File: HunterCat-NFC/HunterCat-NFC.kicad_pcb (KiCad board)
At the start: 2 copper layers, 116.6 x 40.1 mm, 59 parts, among them U1 ATSAMD21E18A, U2 PN7150B0HN/C11004, U3 MCP73831-3-OT, U4 AP2112K-3.3, U5 W25Q32JVSS

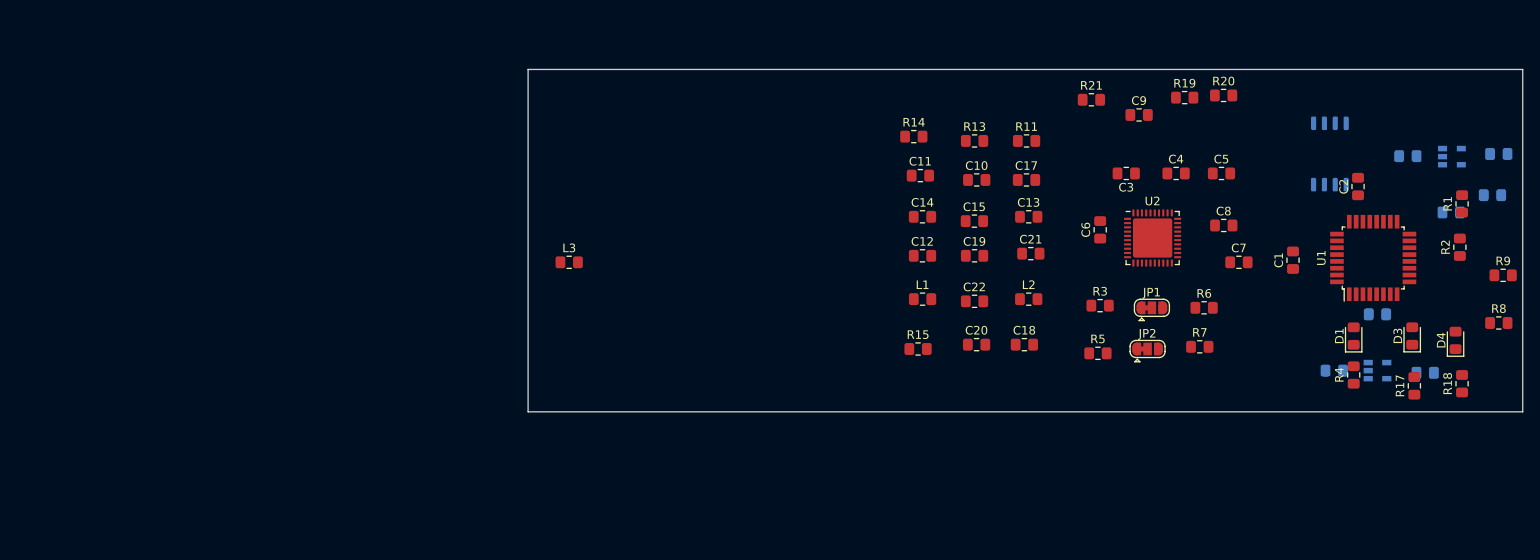
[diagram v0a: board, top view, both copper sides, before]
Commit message: Update libraries, add antenna 30x30mm
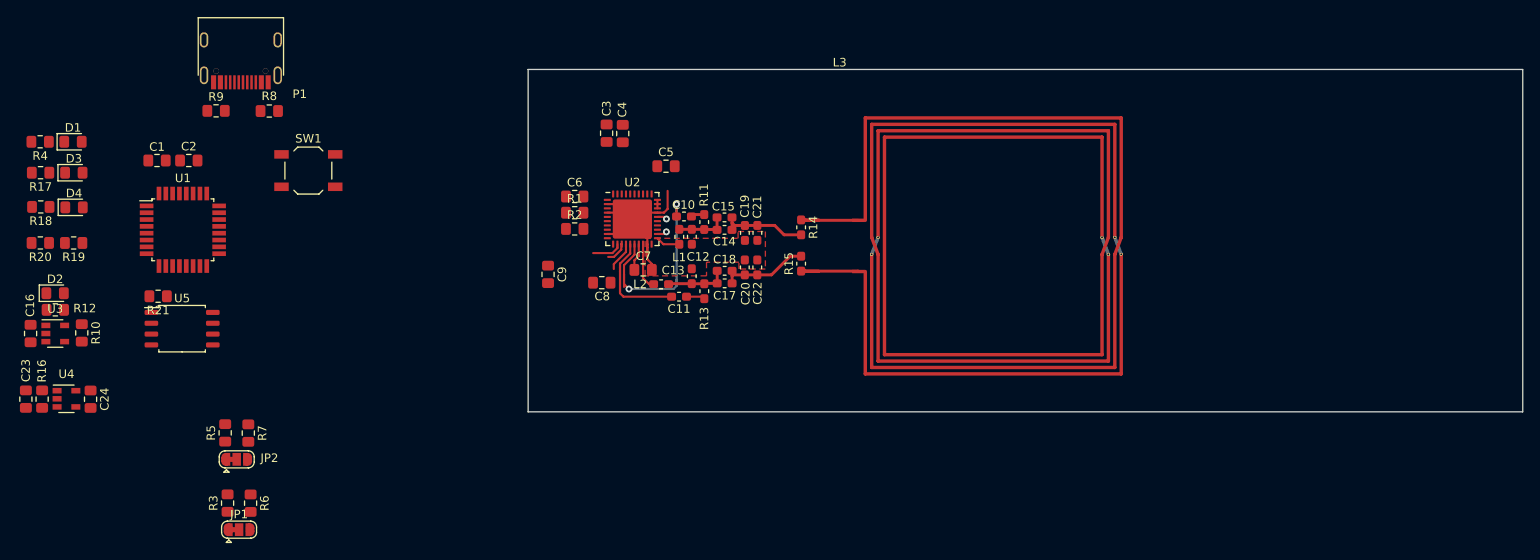
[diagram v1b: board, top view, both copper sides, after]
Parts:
- added P1: USB_C_Plug_USB2.0, Connectors:C393939, F.Cu at (70.2, 74.1)
- added SW1: RESET, Button_Switch_SMD:SW_SPST_TL3342, F.Cu at (78.1, 85.3)
- C10, C11, C12, C13, C14, C15, C17, C18, C19, C20, C21, C22: footprint Capacitor_SMD:C_0805_2012Metric_Pad1.15x1.40mm_HandSolder -> Capacitor_SMD:C_0603_1608Metric_Pad1.05x0.95mm_HandSolder
- C16, C23, C24, D2, R10, R12, R16, U3, U4, U5: moved to F.Cu
- L1, L2: footprint Inductor_SMD:L_0805_2012Metric_Pad1.15x1.40mm_HandSolder -> Inductor_SMD:L_0603_1608Metric_Pad1.05x0.95mm_HandSolder
- L3: footprint Inductor_SMD:L_0805_2012Metric_Pad1.15x1.40mm_HandSolder -> hunter-cat-nfc:NFC-antenna30.4x30.4mm
- R11, R13: footprint Resistor_SMD:R_0805_2012Metric_Pad1.15x1.40mm_HandSolder -> Resistor_SMD:R_0603_1608Metric_Pad1.05x0.95mm_HandSolder
- R14, R15: value 0 -> 3.24R; footprint Resistor_SMD:R_0805_2012Metric_Pad1.15x1.40mm_HandSolder -> Resistor_SMD:R_0603_1608Metric_Pad1.05x0.95mm_HandSolder
- U2: value PN7150B0HN/C11004 -> PN7150B0HN_C11002E-PN7150B0HN_C11002E
- moved R12 170.2 mm to (48.5, 101.6)
- moved D2 168.9 mm to (48.4, 99.6)
- moved R18 167.9 mm to (46.8, 89.5), turned to 180 degrees
- moved U3 165.0 mm to (48.5, 104.4)
- moved R17 163.0 mm to (46.7, 85.5), turned to 180 degrees
- moved C16 162.8 mm to (45.6, 104.4), turned to 90 degrees
- moved D4 162.7 mm to (50.7, 89.6), turned to 0 degrees
- moved R16 162.2 mm to (46.9, 112.0), turned to 270 degrees
- moved R10 161.1 mm to (51.6, 104.3), turned to 270 degrees
- moved D3 158.0 mm to (50.6, 85.5), turned to 0 degrees
- moved R4 156.4 mm to (46.7, 81.9), turned to 180 degrees
- moved U4 153.7 mm to (49.8, 112.0)
- moved C23 153.4 mm to (45.0, 112.0), turned to 270 degrees
- moved R9 152.1 mm to (67.3, 78.3)
- moved D1 151.8 mm to (50.5, 81.9), turned to 0 degrees
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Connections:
- C21 pad 1: Net-(C21-Pad1) -> Net-(C14-Pad1)
- C4 pad 1: Net-(C3-Pad1) -> Net-(C4-Pad1)
- R14 pad 2: Net-(C21-Pad1) -> Net-(C14-Pad1)
- U2 pad 36: Net-(C3-Pad1) -> Net-(C4-Pad1)
- U2 pad 37: Net-(U2-Pad37) -> Net-(C3-Pad1)
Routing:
- net GND: track 0.00 -> 25.6 mm
- net /RXP: track 0.00 -> 24.8 mm, vias 0 -> 2
- net /RXN: track 0.00 -> 15.9 mm
- net Net-(C17-Pad1): track 0.00 -> 10.5 mm
- net Net-(C14-Pad1): track 0.00 -> 10.1 mm
- net Net-(L3-Pad1): track 0.00 -> 8.82 mm
- net Net-(L3-Pad2): track 0.00 -> 8.82 mm
- net Net-(C13-Pad2): track 0.00 -> 7.31 mm
- net Net-(C12-Pad1): track 0.00 -> 5.91 mm
- net /TX2: track 0.00 -> 5.52 mm
- net +BATT: track 0.00 -> 4.71 mm, vias 0 -> 1
- net Net-(C8-Pad1): track 0.00 -> 4.67 mm, vias 0 -> 1
- net Net-(C7-Pad1): track 0.00 -> 3.24 mm
- net /TX1: track 0.00 -> 3.12 mm
- net +3V3: track 0.00 -> 2.59 mm
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- added copper zone on F.Cu, net GND
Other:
- net class Default: trace_width 0.25 -> 0.35

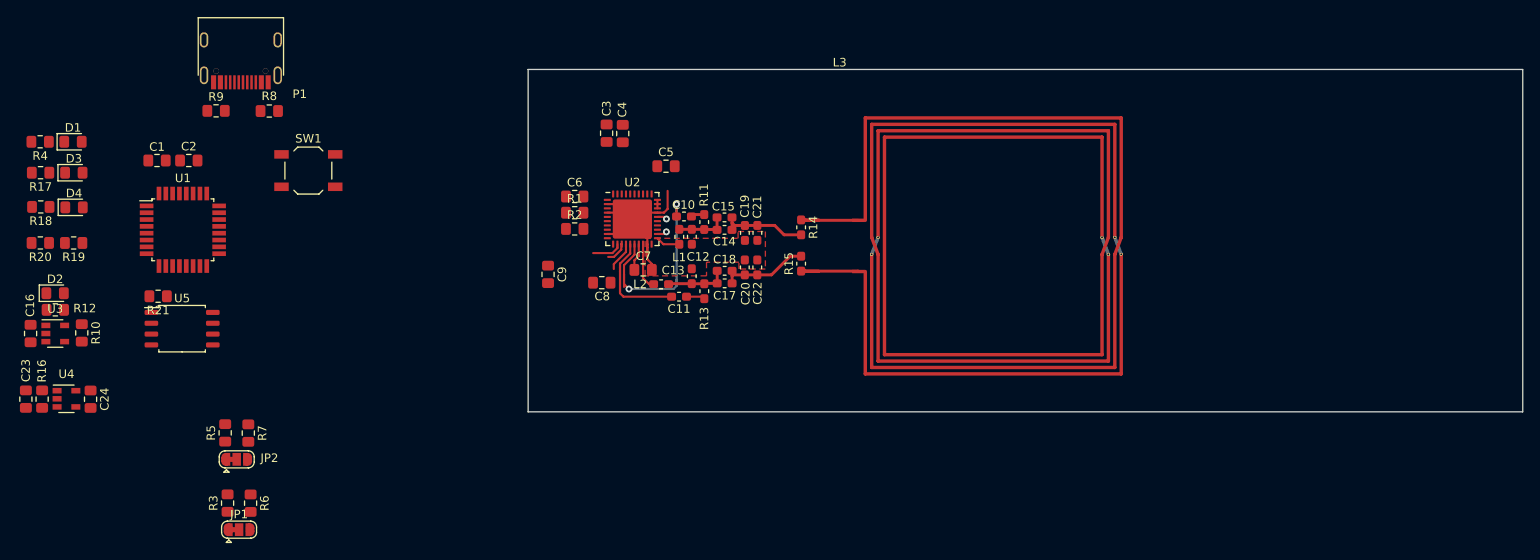
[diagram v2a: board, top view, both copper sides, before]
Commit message: new size for hunter cat family
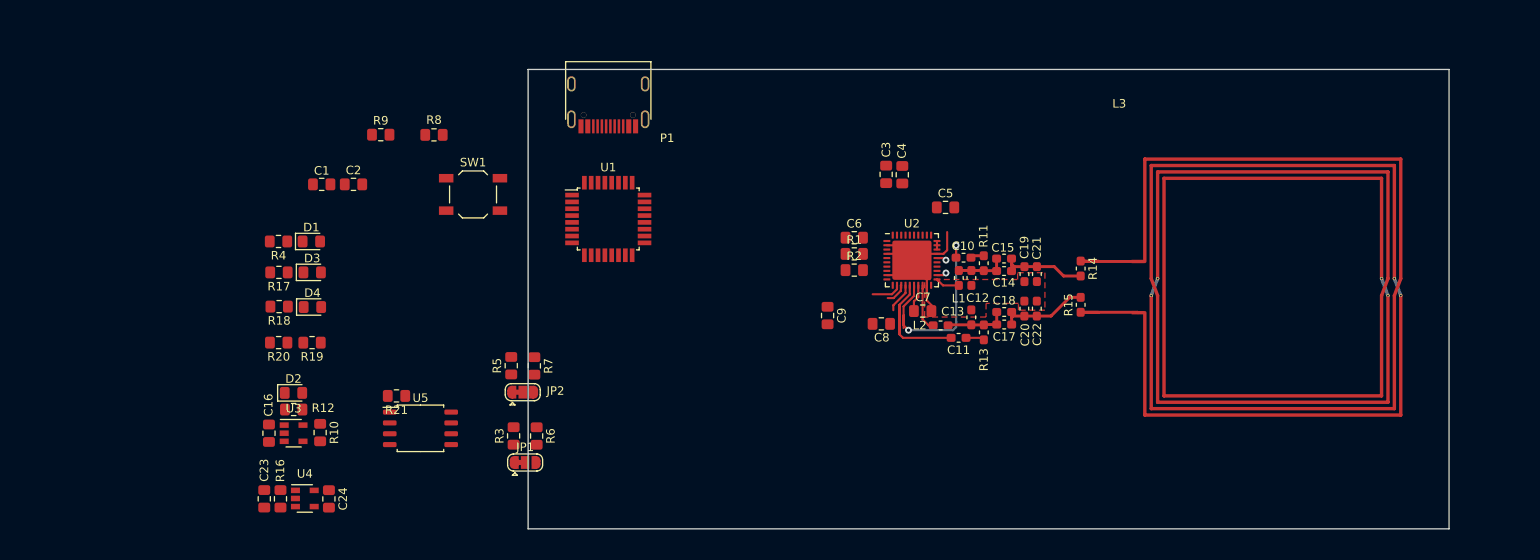
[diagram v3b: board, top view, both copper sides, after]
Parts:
- moved U1 49.9 mm to (113.3, 90.9)
- moved P1 43.4 mm to (113.3, 79.2)
- moved R3 34.4 mm to (102.2, 116.4)
- moved R5 34.4 mm to (101.9, 108.1)
- moved R6 34.4 mm to (104.9, 116.4)
- moved JP1 34.4 mm to (103.5, 119.5)
- moved JP2 34.4 mm to (103.3, 111.2)
- moved R7 34.4 mm to (104.6, 108.2)
- moved C13 33.1 mm to (155.8, 102.5)
- moved C20 33.1 mm to (162.1, 101.4)
- moved C21 33.1 mm to (163.5, 97.4)
- moved C6 33.1 mm to (142.1, 93.1)
- moved C9 33.1 mm to (139.0, 102.3)
- moved L2 33.1 mm to (152.2, 103.4)
- moved R1 33.1 mm to (142.1, 95.0)
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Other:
- board size 116.6 x 40.1 mm -> 108 x 53.8 mm

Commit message: Routeo
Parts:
- moved D2 46.3 mm to (121.6, 121.3), turned to 270 degrees
- moved R12 44.0 mm to (119.6, 121.3), turned to 270 degrees
- moved C16 43.4 mm to (116.9, 118.4), turned to 0 degrees
- moved C1 41.4 mm to (121.0, 84.5)
- moved C2 41.4 mm to (124.7, 84.5)
- moved U3 40.8 mm to (116.9, 121.3), turned to 270 degrees
- moved R10 38.4 mm to (116.9, 124.4), turned to 180 degrees
- moved SW1 38.0 mm to (134.4, 79.4), turned to 180 degrees
- moved C23 37.4 mm to (109.6, 116.2), turned to 0 degrees
- moved R16 36.0 mm to (109.6, 114.3), turned to 0 degrees
- moved R21 35.0 mm to (122.8, 104.9), turned to 0 degrees
- moved U4 34.2 mm to (109.6, 111.5), turned to 90 degrees
- moved U5 33.2 mm to (124.0, 109.8)
- moved C24 32.8 mm to (109.7, 108.6), turned to 0 degrees
- moved D3 32.1 mm to (110.4, 93.0)
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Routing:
- net +3V3: track 2.59 -> 122.8 mm
- net +BATT: track 4.71 -> 105.0 mm, vias 1 -> 4
- net GND: track 25.6 -> 79.4 mm, vias 0 -> 6
- net /VEN: track 0.00 -> 46.2 mm, vias 0 -> 4
- net /ADR1: track 0.00 -> 44.0 mm, vias 0 -> 2
- net /SDA: track 0.00 -> 39.2 mm, vias 0 -> 2
- net /D-: track 0.00 -> 36.4 mm, vias 0 -> 3
- net /IRQ: track 0.00 -> 33.7 mm, vias 0 -> 2
- net /D+: track 0.00 -> 33.2 mm, vias 0 -> 2
- net /ADR0: track 0.00 -> 33.2 mm, vias 0 -> 2
- net /SCL: track 0.00 -> 32.4 mm, vias 0 -> 2
- net /CLK: track 0.00 -> 31.4 mm, vias 0 -> 2
- net /RESET: track 0.00 -> 25.7 mm
- net VBUS: track 0.00 -> 24.6 mm, vias 0 -> 2
- net /MISO: track 0.00 -> 23.4 mm, vias 0 -> 2
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- added copper zone on B.Cu, net GND
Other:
- net class Default: clearance 0.2 -> 0.25; trace_width 0.35 -> 0.3; via_dia 0.8 -> 0.6; via_drill 0.4 -> 0.3
- net class Source added: clearance 0.2, trace_width 0.5, via_dia 0.8, via_drill 0.4
- rule trace_clearance: 0.2 -> 0.25

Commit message: update pcb
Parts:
- added F1: 0.5A, Fuse:Fuse_0805_2012Metric_Pad1.15x1.40mm_HandSolder, F.Cu at (125.8, 85.4)
- added J2: Breakout Conn, Connector_PinSocket_2.54mm:PinSocket_1x06_P2.54mm_Vertical, F.Cu at (148.4, 112.2)
- moved C24 31.9 mm to (137.7, 93.5), turned to 270 degrees
- moved U4 31.1 mm to (134.9, 93.4), turned to 0 degrees
- moved C23 30.6 mm to (130.1, 93.5), turned to 270 degrees
- moved R16 30.6 mm to (132.0, 93.5), turned to 270 degrees
- moved C16 29.9 mm to (118.5, 88.5)
- moved D2 29.9 mm to (123.2, 91.4)
- moved R10 29.9 mm to (118.5, 94.5)
- moved R12 29.9 mm to (121.2, 91.5)
- moved U3 29.9 mm to (118.5, 91.4)
- moved SW1 19.9 mm to (154.2, 77.0)
- moved R21 19.2 mm to (130.8, 122.4), turned to 90 degrees
- moved U5 19.2 mm to (138.0, 122.9)
- moved R9 18.5 mm to (129.5, 85.4)
- moved D1 18.4 mm to (120.4, 104.7)
- moved D3 18.3 mm to (120.4, 108.4)
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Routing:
- net +3V3: track 122.8 -> 2.59 mm
- net +BATT: track 105.0 -> 3.34 mm, vias 4 -> 0
- net GND: track 79.4 -> 30.0 mm, vias 6 -> 0
- net /ADR1: track 44.0 -> 2.25 mm, vias 2 -> 0
- net /VEN: track 46.2 -> 5.15 mm, vias 4 -> 0
- net /SDA: track 39.2 -> 1.02 mm, vias 2 -> 0
- net /D-: track 36.4 -> 0.00 mm, vias 3 -> 0
- net /D+: track 33.2 -> 0.00 mm, vias 2 -> 0
- net /ADR0: track 33.2 -> 1.20 mm, vias 2 -> 0
- net /SCL: track 32.4 -> 1.61 mm, vias 2 -> 0
- net /CLK: track 31.4 -> 1.83 mm, vias 2 -> 0
- net /IRQ: track 33.7 -> 5.20 mm, vias 2 -> 0
- net /RESET: track 25.7 -> 0.00 mm
- net VBUS: track 24.6 -> 0.00 mm, vias 2 -> 0
- net /MISO: track 23.4 -> 0.00 mm, vias 2 -> 0
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
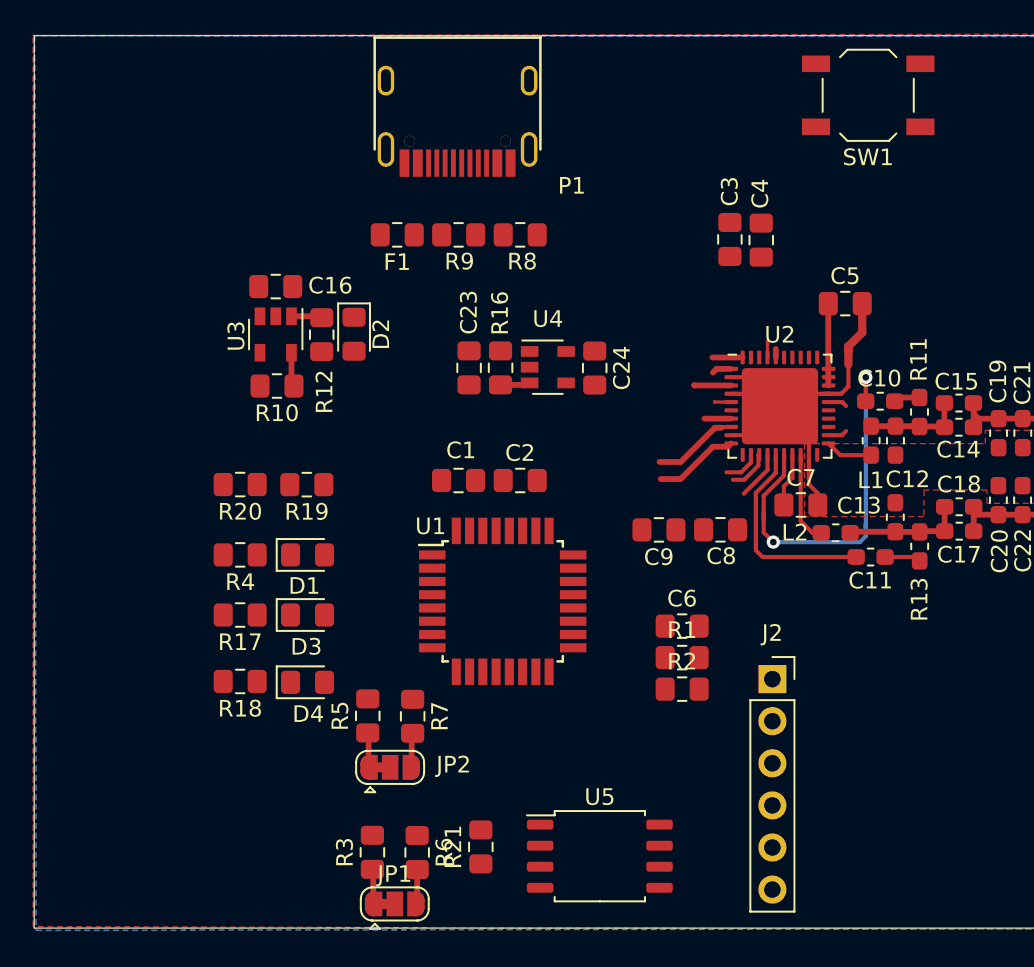
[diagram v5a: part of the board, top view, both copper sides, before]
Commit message: add footprint crystal and battery connector
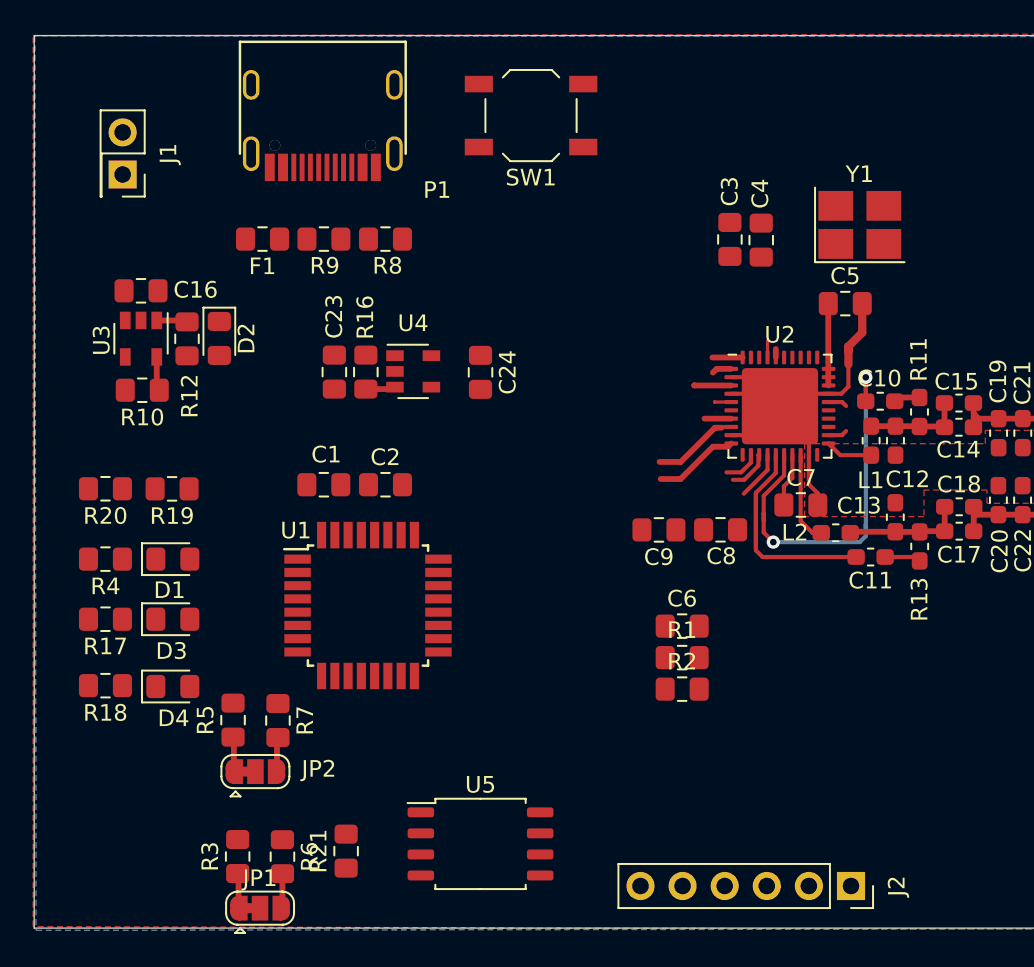
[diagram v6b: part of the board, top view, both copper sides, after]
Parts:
- added J1: Battery, Connector_PinSocket_2.54mm:PinSocket_2x01_P2.54mm_Vertical, F.Cu at (109.2, 81.8)
- added Y1: 27.12Mhz, Crystal:Crystal_SMD_3225-4Pin_3.2x2.5mm_HandSoldering, F.Cu at (153.7, 84.8)
- moved SW1 20.4 mm to (133.9, 78.2)
- moved J2 13.4 mm to (153.2, 124.7), turned to 270 degrees
- moved C1 8.13 mm to (121.4, 100.5)
- moved C2 8.13 mm to (125.1, 100.5)
- moved R16 8.13 mm to (123.9, 93.7)
- moved R21 8.13 mm to (122.7, 122.6)
- moved R8 8.13 mm to (125.1, 85.7)
- moved R9 8.13 mm to (121.4, 85.7)
- moved C16 8.13 mm to (110.3, 88.8)
- moved C23 8.13 mm to (122.0, 93.7)
- moved D1 8.13 mm to (112.2, 105.0)
- moved D2 8.13 mm to (115.1, 91.7)
- moved D3 8.13 mm to (112.2, 108.6)
- moved D4 8.13 mm to (112.2, 112.7)
- moved F1 8.13 mm to (117.7, 85.7)
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
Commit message: fix routeo
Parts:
- moved R3 37.2 mm to (137.1, 92.2)
- moved JP1 37.2 mm to (138.4, 95.3)
- moved R6 37.2 mm to (139.8, 92.2)
- moved R5 36.4 mm to (137.1, 85.1)
- moved R7 36.4 mm to (139.8, 85.1)
- moved JP2 36.4 mm to (138.4, 88.2)
- moved C1 16.0 mm to (118.7, 116.3), turned to 90 degrees
- moved C2 0.47 mm to (125.2, 100.1)
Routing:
- net +3V3: track 2.59 -> 161.8 mm, vias 0 -> 5
- net /SCL: track 1.61 -> 100.5 mm, vias 0 -> 4
- net +BATT: track 3.34 -> 88.3 mm, vias 0 -> 6
- net /SDA: track 1.02 -> 83.7 mm, vias 0 -> 4
- net /IRQ: track 5.20 -> 86.8 mm, vias 0 -> 3
- net GND: track 30.0 -> 97.0 mm, vias 0 -> 9
- net /VEN: track 5.15 -> 69.9 mm, vias 0 -> 2
- net /RESET: track 0.00 -> 39.0 mm
- net /CLK: track 1.83 -> 40.7 mm, vias 0 -> 2
- net VBUS: track 0.00 -> 36.7 mm
- net /D-: track 0.00 -> 36.1 mm, vias 0 -> 2
- net /D+: track 0.00 -> 35.2 mm, vias 0 -> 2
- net /CS: track 0.00 -> 25.8 mm, vias 0 -> 2
- net Net-(C3-Pad1): track 1.01 -> 23.6 mm
- net /SCK: track 0.00 -> 22.2 mm, vias 0 -> 2
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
